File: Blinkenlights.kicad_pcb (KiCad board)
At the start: 2 copper layers, 56.6 x 69.1 mm, 32 parts, among them J1 6502_socket, J2 Conn_02x24_Odd_Even, J3 Conn_02x03_Odd_Even, U1 WD65C02, U2 ULN2803A, U3 ULN2803A, U4 ULN2803A

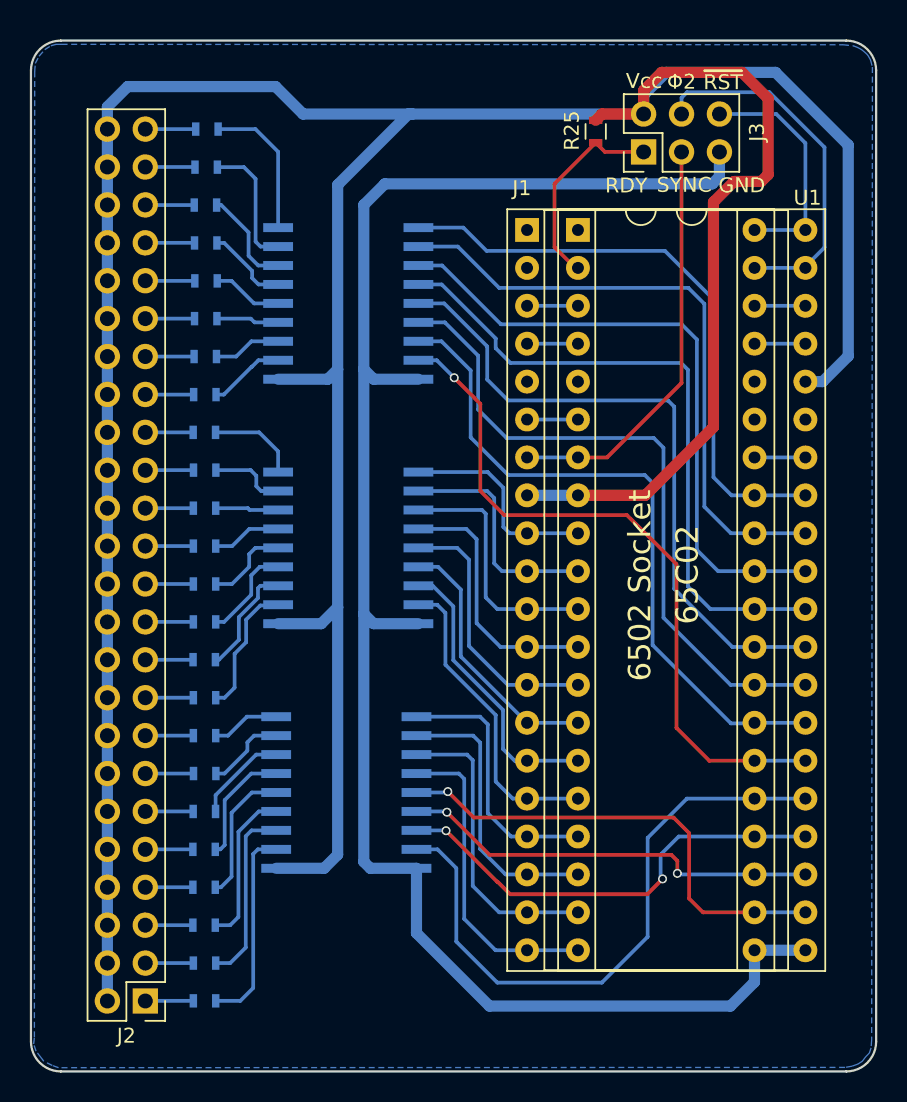
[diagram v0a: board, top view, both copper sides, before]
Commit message: Added text to PCB
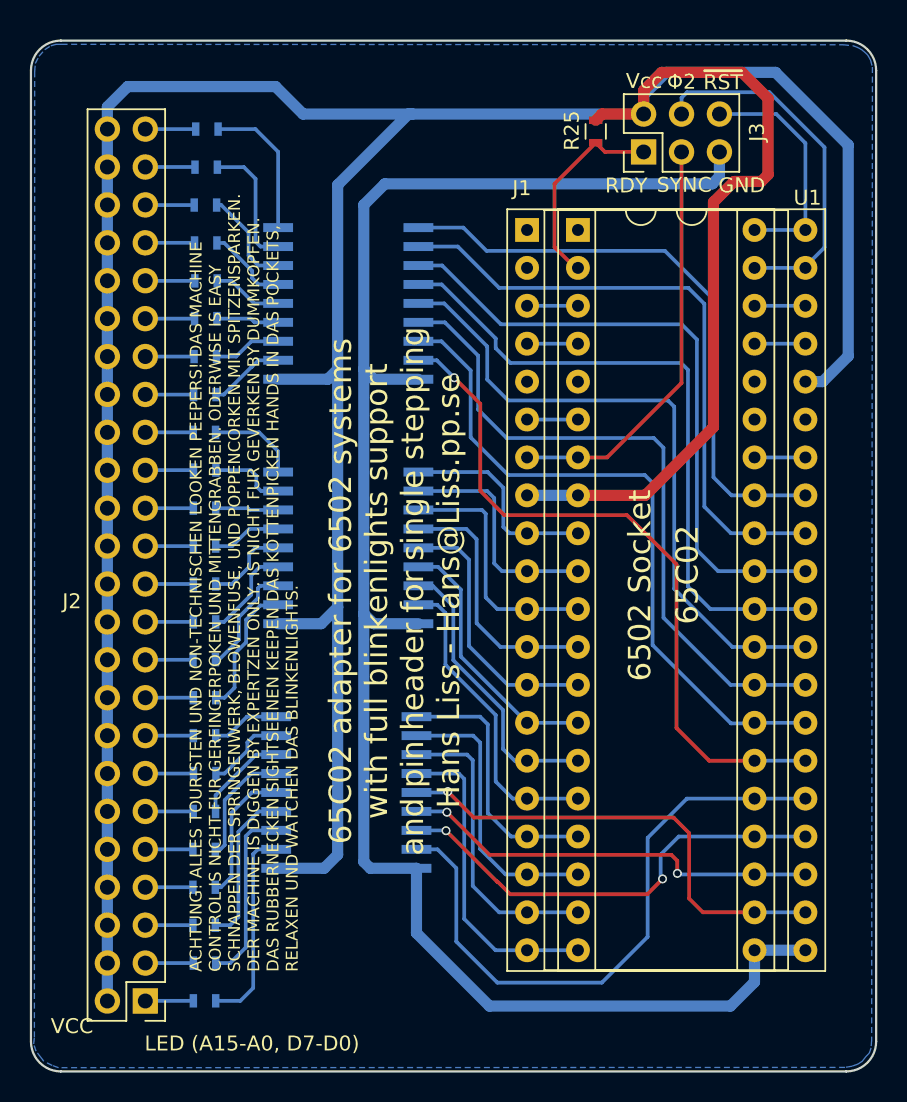
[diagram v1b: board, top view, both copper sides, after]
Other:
- board text added: "65C02 adapter for 6502 systems with full blinkenlights support and pin header for single stepping Hans Liss - Hans@Liss.pp.se"
- board text added: "ACHTUNG! ALLES TOURISTEN UND NON-TECHNISCHEN LOOKEN PEEPERS! DAS MACHINE CONTROL IS NICHT FUR GERFINGERPOKEN UND MITTENGRABBEN. ODERWISE IS EASY SCHNAPPEN DER SPRINGENWERK, BLOWENFUSE, UND POPPENCORKEN MIT SPITZENSPARKEN. DER MACHINE IS DIGGEN BY EXPERTZEN ONLY. IS NICHT FUR GEVERKEN BY DUMMKOPFEN. DAS RUBBERNECKEN SIGHTSEENEN KEEPEN DAS KOTTENPICKEN HANDS IN DAS POCKETS, RELAXEN UND WATCHEN DAS 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"
- board text added: "LED (A15-A0, D7-D0)"
- board text added: "VCC"
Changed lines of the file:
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@@
     (area 46.244999 67.404999 103.025001 136.625001)
     (thickness 1.6)
-    (drawings 22)
+    (drawings 26)
     (tracks 447)
     (zones 0)
@@
     (pad_to_mask_clearance 0.2)
     (aux_axis_origin 0 0)
-    (visible_elements FFFFFF7F)
+    (visible_elements 7FFFFFFF)
     (pcbplotparams
       (layerselection 0x3f0fc_80000001)
@@
     (descr "Through hole straight pin header, 2x24, 2.54mm pitch, double rows")
     (tags "Through hole pin header THT 2x24 2.54mm double row")
-    (fp_text reference J2 (at 1.27 -2.33 180) (layer F.SilkS)
+    (fp_text reference J2 (at 4.92 26.78 180) (layer F.SilkS)
       (effects (font (size 1 1) (thickness 0.15)))
     )
@@
     )
   )
+  (gr_text "65C02 adapter for 6502 systems\nwith full blinkenlights support\nand pin header for single stepping\nHans Liss - Hans@Liss.pp.se" (at 70.69 104.37 90) (layer F.SilkS)
+    (effects (font (size 1.5 1.5) (thickness 0.3)))
+  )
+  (gr_text "LED (A15-A0, D7-D0)" (at 61.13 134.68) (layer F.SilkS)
+    (effects (font (size 1 1) (thickness 0.2)))
+  )
+  (gr_text VCC (at 49.07 133.52) (layer F.SilkS)
+    (effects (font (size 1 1) (thickness 0.2)))
+  )
+  (gr_text "ACHTUNG! ALLES TOURISTEN UND NON-TECHNISCHEN LOOKEN PEEPERS! DAS MACHINE\nCONTROL IS NICHT FUR GERFINGERPOKEN UND MITTENGRABBEN. ODERWISE IS EASY\nSCHNAPPEN DER SPRINGENWERK, BLOWENFUSE, UND POPPENCORKEN MIT SPITZENSPARKEN.\nDER MACHINE IS DIGGEN BY EXPERTZEN ONLY. IS NICHT FUR GEVERKEN BY DUMMKOPFEN.\nDAS RUBBERNECKEN SIGHTSEENEN KEEPEN DAS KOTTENPICKEN HANDS IN DAS POCKETS,\nRELAXEN UND WATCHEN DAS BLINKENLIGHTS." (at 60.6 129.88 90) (layer F.SilkS)
+    (effects (font (size 0.8 0.8) (thickness 0.1)) (justify left))
+  )
   (gr_arc (start 48.32 134.55) (end 48.32 136.55) (angle 90) (layer Edge.Cuts) (width 0.15))
